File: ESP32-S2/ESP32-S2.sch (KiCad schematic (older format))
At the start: 45 parts, among them IC1 IP4220CZ6, J1 USB_A, J2 TYPE-C-31-M-12, J3 Conn_01x18_Male, J4 S2B-PH-SM4-TB(LF)(SN), J5 Conn_01x22_Male, SW1 SW_Push, SW2 SW_Push, U1 ESP32-S2-WROOM-ESP32-S2-WROOM, U2 MMBT8050, U3 MMBT8050, U4 MCP73831-2-OT, U5 AMS1117-3.3, U6 CH340C

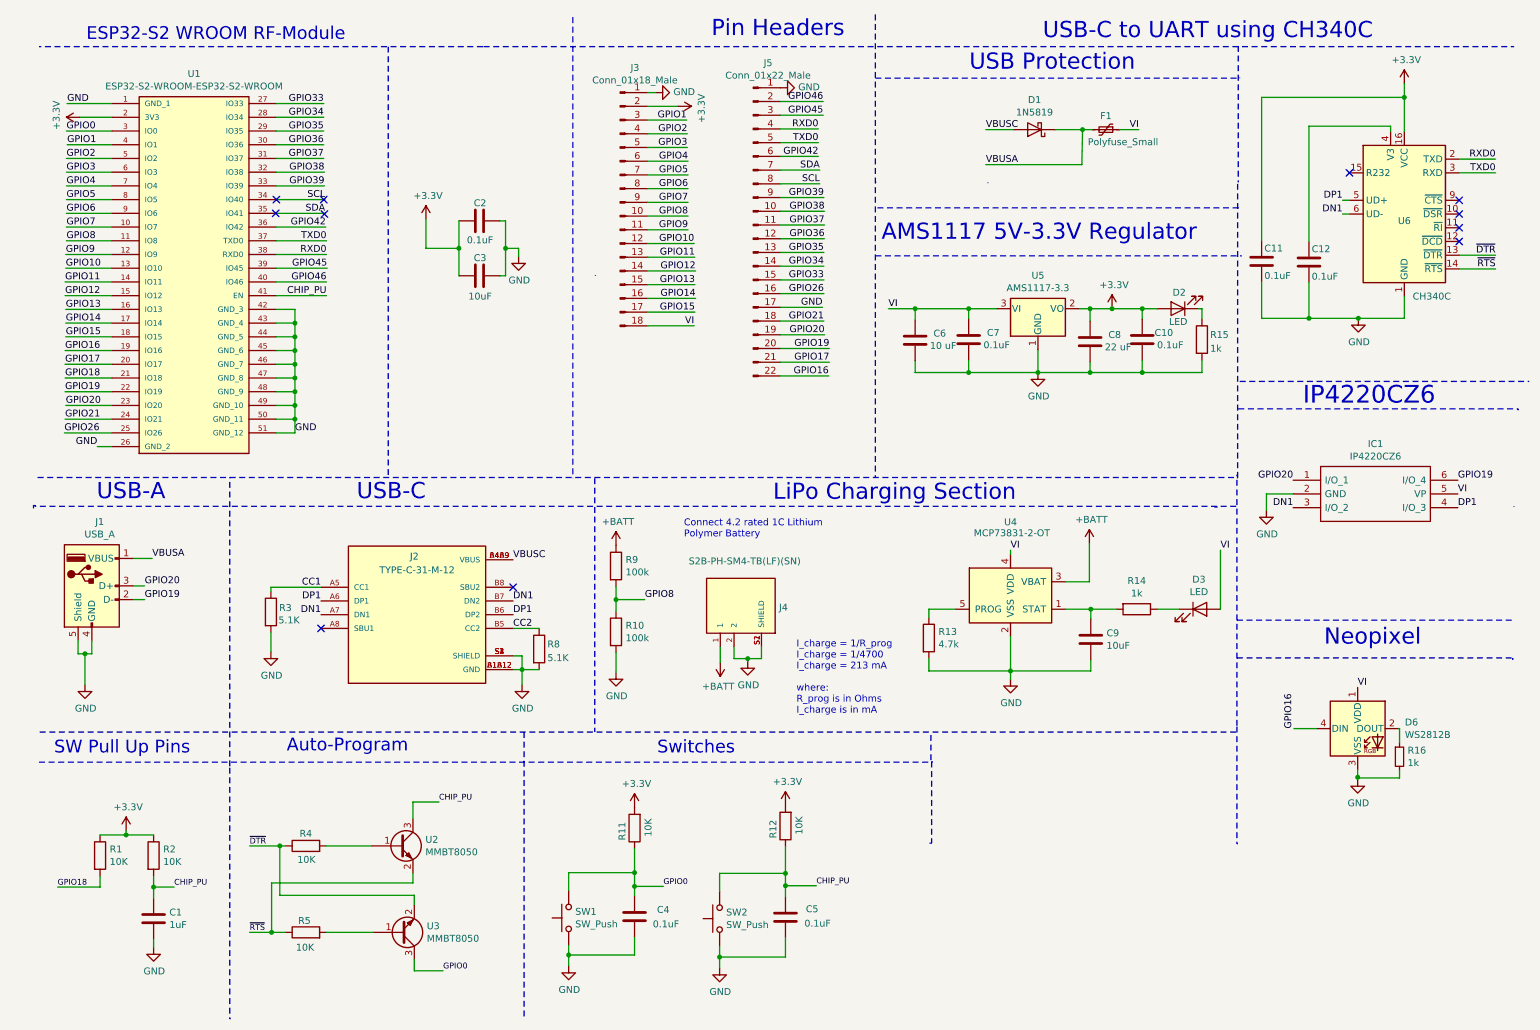
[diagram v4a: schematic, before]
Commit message: Routed 4-layer v.2.1
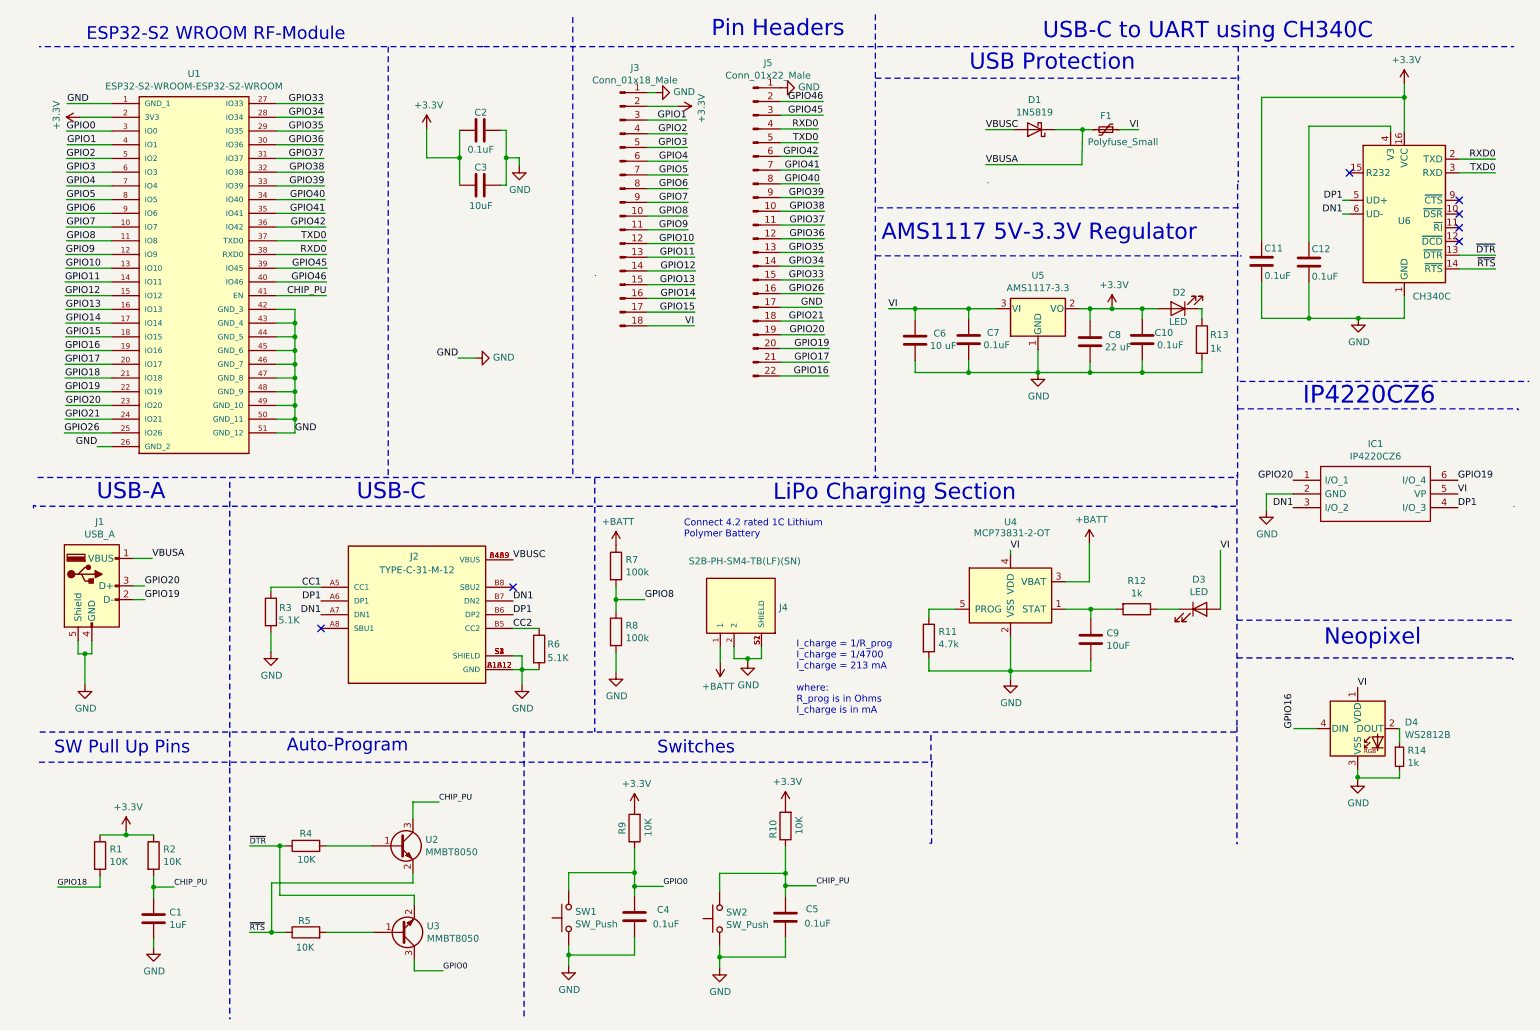
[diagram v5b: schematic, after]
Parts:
- renumbered D6 to D4, R12 to R10, R13 to R11, R14 to R12, R15 to R13, R16 to R14, R8 to R6, R9 to R7, R10 to R8, R11 to R9
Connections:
- net SCL renamed GPIO40
- net SDA renamed GPIO41
- no-connect marks 11 -> 7
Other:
- moved on the sheet: C2, C3
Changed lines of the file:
@@
 GPIO0
 Wire Wire Line
-	3830 1985 3870 1985
-Wire Wire Line
-	3290 2185 3530 2185
-Wire Wire Line
-	3290 1975 3290 2185
-Wire Wire Line
-	3530 2185 3530 2385
-Connection ~ 3530 2185
-Wire Wire Line
-	3530 1985 3530 2185
+	3835 1325 3875 1325
+Wire Wire Line
+	3295 1525 3535 1525
+Wire Wire Line
+	3295 1315 3295 1525
+Wire Wire Line
+	3535 1525 3535 1725
+Connection ~ 3535 1525
+Wire Wire Line
+	3535 1325 3535 1525
 $Comp
 L power:+3.3V #PWR06
 U 1 1 6005C874
-P 3290 1975
-F 0 "#PWR06" H 3290 1825 50  0001 C CNN
-F 1 "+3.3V" H 3305 2148 50  0000 C CNN
-F 2 "" H 3290 1975 50  0001 C CNN
-F 3 "" H 3290 1975 50  0001 C CNN
-	1    3290 1975
+P 3295 1315
+F 0 "#PWR06" H 3295 1165 50  0001 C CNN
+F 1 "+3.3V" H 3310 1488 50  0000 C CNN
+F 2 "" H 3295 1315 50  0001 C CNN
+F 3 "" H 3295 1315 50  0001 C CNN
+	1    3295 1315
 	1    0    0    -1
 $EndComp
@@
 L Device:C C2
 U 1 1 60022F39
-P 3680 1985
-F 0 "C2" V 3810 1935 50  0000 L CNN
-F 1 "0.1uF" V 3540 1885 50  0000 L CNN
-F 2 "Capacitor_SMD:C_0603_1608Metric" H 3718 1835 50  0001 C CNN
-F 3 "~" H 3680 1985 50  0001 C CNN
-	1    3680 1985
+P 3685 1325
+F 0 "C2" V 3815 1275 50  0000 L CNN
+F 1 "0.1uF" V 3545 1225 50  0000 L CNN
+F 2 "Capacitor_SMD:C_0603_1608Metric" H 3723 1175 50  0001 C CNN
+F 3 "~" H 3685 1325 50  0001 C CNN
+	1    3685 1325
 	0    -1   -1   0
 $EndComp
@@
 L Device:C C3
 U 1 1 60021E18
-P 3680 2385
-F 0 "C3" V 3810 2335 50  0000 L CNN
-F 1 "10uF" V 3530 2295 50  0000 L CNN
-F 2 "Capacitor_SMD:C_0603_1608Metric" H 3718 2235 50  0001 C CNN
-F 3 "~" H 3680 2385 50  0001 C CNN
-	1    3680 2385
+P 3685 1725
+F 0 "C3" V 3815 1675 50  0000 L CNN
+F 1 "10uF" V 3535 1635 50  0000 L CNN
+F 2 "Capacitor_SMD:C_0603_1608Metric" H 3723 1575 50  0001 C CNN
+F 3 "~" H 3685 1725 50  0001 C CNN
+	1    3685 1725
 	0    -1   -1   0
 $EndComp
@@
 Wire Wire Line
 	2200 2030 2560 2030
-Wire Wire Line
-	2200 1930 2555 1930
-Text Label 2555 1930 2    50   ~ 0
-SDA
-Wire Wire Line
-	2200 1830 2555 1830
-Text Label 2555 1830 2    50   ~ 0
-SCL
 Text Label 2565 2430 2    50   ~ 0
 GPIO46
@@
 	430  4055 430  4080
 Wire Wire Line
-	3870 1985 3870 2185
-$Comp
-L power:GND #PWR09
+	3875 1325 3875 1525
+$Comp
+L power:GND #PWR08
 U 1 1 600B09CA
-P 3965 2245
-F 0 "#PWR09" H 3965 1995 50  0001 C CNN
-F 1 "GND" H 3970 2072 50  0000 C CNN
-F 2 "" H 3965 2245 50  0001 C CNN
-F 3 "" H 3965 2245 50  0001 C CNN
-	1    3965 2245
-	1    0    0    -1
-$EndComp
-Wire Wire Line
-	3965 2185 3870 2185
-Connection ~ 3870 2185
-Wire Wire Line
-	3870 2185 3870 2385
+P 3970 1585
+F 0 "#PWR08" H 3970 1335 50  0001 C CNN
+F 1 "GND" H 3975 1412 50  0000 C CNN
+F 2 "" H 3970 1585 50  0001 C CNN
+F 3 "" H 3970 1585 50  0001 C CNN
+	1    3970 1585
+	1    0    0    -1
+$EndComp
+Wire Wire Line
+	3970 1525 3875 1525
+Connection ~ 3875 1525
+Wire Wire Line
+	3875 1525 3875 1725
 Wire Wire Line
 	2200 3530 2335 3530
@@
 	1000 3630 895  3630
 Wire Wire Line
-	3965 2185 3965 2245
+	3970 1525 3970 1585
 Text Label 895  3630 2    50   ~ 0
 GND
@@
 $EndComp
 $Comp
-L Device:R R11
+L Device:R R9
 U 1 1 60282C1A
 P 4810 6410
-F 0 "R11" V 4900 6365 50  0000 L CNN
+F 0 "R9" V 4900 6365 50  0000 L CNN
 F 1 "10K" V 4710 6340 50  0000 L CNN
 F 2 "Resistor_SMD:R_0603_1608Metric" V 4740 6410 50  0001 C CNN
@@
 CHIP_PU
 $Comp
-L Device:R R12
+L Device:R R10
 U 1 1 602B227B
 P 5910 6395
-F 0 "R12" V 6000 6350 50  0000 L CNN
+F 0 "R10" V 6000 6350 50  0000 L CNN
 F 1 "10K" V 5810 6325 50  0000 L CNN
 F 2 "Resistor_SMD:R_0603_1608Metric" V 5840 6395 50  0001 C CNN
@@
 Wire Wire Line
 	5875 3115 6225 3115
-NoConn ~ 2545 1830
-NoConn ~ 2550 1935
 Wire Wire Line
 	4905 1050 4965 1050
-NoConn ~ 2200 1830
-NoConn ~ 2195 1930
 $Comp
 L Device:R R4
@@
 VBUSC
 $Comp
-L power:GND #PWR08
+L power:GND #PWR09
 U 1 1 606D1B6E
 P 3990 5365
-F 0 "#PWR08" H 3990 5115 50  0001 C CNN
+F 0 "#PWR09" H 3990 5115 50  0001 C CNN
 F 1 "GND" H 3995 5192 50  0000 C CNN
 F 2 "" H 3990 5365 50  0001 C CNN
@@
 $EndComp
 $Comp
-L Device:R R8
+L Device:R R6
 U 1 1 600D9660
 P 4115 5105
-F 0 "R8" H 4175 5140 50  0000 L CNN
+F 0 "R6" H 4175 5140 50  0000 L CNN
 F 1 "5.1K" H 4175 5040 50  0000 L CNN
 F 2 "Resistor_SMD:R_0603_1608Metric" V 4045 5105 50  0001 C CNN
@@
 $EndComp
 Wire Wire Line
-	3830 2385 3870 2385
+	3835 1725 3875 1725
 Wire Wire Line
 	8945 3090 8945 3000
 $Comp
-L Device:R R15
+L Device:R R13
 U 1 1 6033F05F
 P 8945 2850
-F 0 "R15" H 9005 2885 50  0000 L CNN
+F 0 "R13" H 9005 2885 50  0000 L CNN
 F 1 "1k" H 9005 2785 50  0000 L CNN
 F 2 "Resistor_SMD:R_0603_1608Metric" V 8875 2850 50  0001 C CNN
@@
 	4905 2750 5245 2750
 Text Label 6160 1615 2    50   ~ 0
-SDA
+GPIO41
 Text Label 6160 1715 2    50   ~ 0
-SCL
+GPIO40
 Wire Wire Line
 	5875 1615 6160 1615
@@
 $EndComp
 $Comp
-L Device:R_Small R16
+L Device:R_Small R14
 U 1 1 60CA2577
 P 10385 5890
-F 0 "R16" H 10444 5936 50  0000 L CNN
+F 0 "R14" H 10444 5936 50  0000 L CNN
 F 1 "1k" H 10444 5845 50  0000 L CNN
 F 2 "Resistor_SMD:R_0603_1608Metric" H 10385 5890 50  0001 C CNN
@@
 Neopixel
 $Comp
-L Device:R R13
+L Device:R R11
 U 1 1 60A58974
 P 6955 5025
-F 0 "R13" H 7025 5071 50  0000 L CNN
+F 0 "R11" H 7025 5071 50  0000 L CNN
 F 1 "4.7k" H 7025 4980 50  0000 L CNN
 F 2 "Resistor_SMD:R_0603_1608Metric" V 6885 5025 50  0001 C CNN
@@
 $EndComp
 $Comp
-L Device:R R14
+L Device:R R12
 U 1 1 60A59CD2
 P 8470 4815
-F 0 "R14" V 8263 4815 50  0000 C CNN
+F 0 "R12" V 8263 4815 50  0000 C CNN
 F 1 "1k" V 8354 4815 50  0000 C CNN
 F 2 "Resistor_SMD:R_0603_1608Metric" V 8400 4815 50  0001 C CNN
@@
 $EndComp
 $Comp
-L Device:R R10
+L Device:R R8
 U 1 1 60AABA38
 P 4675 4980
-F 0 "R10" H 4745 5026 50  0000 L CNN
+F 0 "R8" H 4745 5026 50  0000 L CNN
 F 1 "100k" H 4745 4935 50  0000 L CNN
 F 2 "Resistor_SMD:R_0603_1608Metric" V 4605 4980 50  0001 C CNN
@@
 $EndComp
 $Comp
-L Device:R R9
+L Device:R R7
 U 1 1 60AC2C56
 P 4675 4500
-F 0 "R9" H 4745 4546 50  0000 L CNN
+F 0 "R7" H 4745 4546 50  0000 L CNN
 F 1 "100k" H 4745 4455 50  0000 L CNN
 F 2 "Resistor_SMD:R_0603_1608Metric" V 4605 4500 50  0001 C CNN
@@
 $EndComp
 $Comp
-L LED:WS2812B D6
+L LED:WS2812B D4
 U 1 1 609FC678
 P 10080 5685
-F 0 "D6" H 10424 5731 50  0000 L CNN
+F 0 "D4" H 10424 5731 50  0000 L CNN
 F 1 "WS2812B" H 10424 5640 50  0000 L CNN
 F 2 "WS2018:WS2812B2020" H 10130 5385 50  0001 L TNN
@@
 	1    0    0    1
 $EndComp
+Text Label 2555 1830 2    50   ~ 0
+GPIO40
+Wire Wire Line
+	2200 1830 2555 1830
+Text Label 2555 1930 2    50   ~ 0
+GPIO41
+Wire Wire Line
+	2200 1930 2555 1930
+$Comp
+L power:GND #PWR07
+U 1 1 60A90427
+P 3650 2985
+F 0 "#PWR07" H 3650 2735 50  0001 C CNN
+F 1 "GND" V 3655 2857 50  0000 R CNN
+F 2 "" H 3650 2985 50  0001 C CNN
+F 3 "" H 3650 2985 50  0001 C CNN
+	1    3650 2985
+	0    -1   -1   0
+$EndComp
+Wire Wire Line
+	3650 2985 3525 2985
+Text Label 3525 2985 2    50   ~ 0
+GND
 $EndSCHEMATC

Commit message: Routing 4-Layer v3.0
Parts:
- C1, C10, C11, C12, C2, C3, C4, C5, C6, C7, C8, C9: symbol Device:C -> ESP32-S2-rescue:C-Device
- D1: symbol Diode:1N5819 -> ESP32-S2-rescue:1N5819-Diode
- D2, D3: symbol Device:LED -> ESP32-S2-rescue:LED-Device
- D4: symbol LED:WS2812B -> ESP32-S2-rescue:WS2812B-LED
- F1: symbol Device:Polyfuse_Small -> ESP32-S2-rescue:Polyfuse_Small-Device
- J3: symbol Connector:Conn_01x18_Male -> ESP32-S2-rescue:Conn_01x18_Male-Connector
- J5: symbol Connector:Conn_01x22_Male -> ESP32-S2-rescue:Conn_01x22_Male-Connector
- R1, R10, R11, R12, R13, R2, R3, R4, R5, R6, R7, R8, R9: symbol Device:R -> ESP32-S2-rescue:R-Device
- R14: symbol Device:R_Small -> ESP32-S2-rescue:R_Small-Device
- SW1, SW2: symbol Switch:SW_Push -> ESP32-S2-rescue:SW_Push-Switch
- U4: symbol Battery_Management:MCP73831-2-OT -> ESP32-S2-rescue:MCP73831-2-OT-Battery_Management
- U5: symbol Regulator_Linear:AMS1117-3.3 -> ESP32-S2-rescue:AMS1117-3.3-Regulator_Linear
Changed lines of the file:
@@
 $EndDescr
 $Comp
-L power:GND #PWR010
+L ESP32-S2-rescue:GND-power #PWR010
 U 1 1 6010A754
 P 4330 7415
@@
 $EndComp
 $Comp
-L power:GND #PWR016
+L ESP32-S2-rescue:GND-power #PWR016
 U 1 1 6010BC5F
 P 5430 7430
@@
 	5430 7270 5430 7350
 $Comp
-L Device:C C4
+L ESP32-S2-rescue:C-Device C4
 U 1 1 60115502
 P 4810 7055
@@
 $EndComp
 $Comp
-L Device:C C5
+L ESP32-S2-rescue:C-Device C5
 U 1 1 60116DC7
 P 5910 7060
@@
 	3535 1325 3535 1525
 $Comp
-L power:+3.3V #PWR06
+L ESP32-S2-rescue:+3.3V-power #PWR06
 U 1 1 6005C874
 P 3295 1315
@@
 $EndComp
 $Comp
-L Device:C C2
+L ESP32-S2-rescue:C-Device C2
 U 1 1 60022F39
 P 3685 1325
@@
 $EndComp
 $Comp
-L Device:C C3
+L ESP32-S2-rescue:C-Device C3
 U 1 1 60021E18
 P 3685 1725
@@
 GPIO35
 $Comp
-L power:GND #PWR027
+L ESP32-S2-rescue:GND-power #PWR027
 U 1 1 60107D6F
 P 10085 2695
@@
 	3875 1325 3875 1525
 $Comp
-L power:GND #PWR08
+L ESP32-S2-rescue:GND-power #PWR08
 U 1 1 600B09CA
 P 3970 1585
@@
 $EndComp
 $Comp
-L Device:R R9
+L ESP32-S2-rescue:R-Device R9
 U 1 1 60282C1A
 P 4810 6410
@@
 CHIP_PU
 $Comp
-L Device:R R10
+L ESP32-S2-rescue:R-Device R10
 U 1 1 602B227B
 P 5910 6395
@@
 NoConn ~ 10820 1935
 $Comp
-L Device:C C12
+L ESP32-S2-rescue:C-Device C12
 U 1 1 600DA2FD
 P 9725 2285
@@
 	805  5140 855  5140
 $Comp
-L power:GND #PWR02
+L ESP32-S2-rescue:GND-power #PWR02
 U 1 1 6048FF18
 P 805 5365
@@
 	1105 6430 1105 6460
 $Comp
-L power:+3.3V #PWR03
+L ESP32-S2-rescue:+3.3V-power #PWR03
 U 1 1 600E7114
 P 1105 6430
@@
 	1305 7220 1305 7280
 $Comp
-L power:GND #PWR04
+L ESP32-S2-rescue:GND-power #PWR04
 U 1 1 600DA8F4
 P 1305 7280
@@
 $EndComp
 $Comp
-L Device:C C1
+L ESP32-S2-rescue:C-Device C1
 U 1 1 600D7FAA
 P 1305 7070
@@
 $EndComp
 $Comp
-L Device:R R2
+L ESP32-S2-rescue:R-Device R2
 U 1 1 600D7B61
 P 1305 6610
@@
 $EndComp
 $Comp
-L Device:R R1
+L ESP32-S2-rescue:R-Device R1
 U 1 1 600D7356
 P 915 6610
@@
 	4905 1250 5190 1250
 $Comp
-L power:GND #PWR014
+L ESP32-S2-rescue:GND-power #PWR014
 U 1 1 60579A17
 P 4965 1050
@@
 	4905 1050 4965 1050
 $Comp
-L Device:R R4
+L ESP32-S2-rescue:R-Device R4
 U 1 1 6015B31B
 P 2415 6540
@@
 $EndComp
 $Comp
-L Device:R R5
+L ESP32-S2-rescue:R-Device R5
 U 1 1 6015D1FA
 P 2415 7170
@@
 Auto-Program\n
 $Comp
-L power:+3.3V #PWR020
+L ESP32-S2-rescue:+3.3V-power #PWR020
 U 1 1 602B0D1F
 P 5910 6245
@@
 $EndComp
 $Comp
-L power:+3.3V #PWR013
+L ESP32-S2-rescue:+3.3V-power #PWR013
 U 1 1 602AFFC8
 P 4810 6260
@@
 VBUSC
 $Comp
-L power:GND #PWR09
+L ESP32-S2-rescue:GND-power #PWR09
 U 1 1 606D1B6E
 P 3990 5365
@@
 $EndComp
 $Comp
-L Device:R R6
+L ESP32-S2-rescue:R-Device R6
 U 1 1 600D9660
 P 4115 5105
@@
 $EndComp
 $Comp
-L Device:R R3
+L ESP32-S2-rescue:R-Device R3
 U 1 1 600D889F
 P 2160 4835
@@
 Pin Headers
 $Comp
-L Regulator_Linear:AMS1117-3.3 U5
+L ESP32-S2-rescue:AMS1117-3.3-Regulator_Linear U5
 U 1 1 6028A484
 P 7750 2625
@@
 VI
 $Comp
-L Device:C C7
+L ESP32-S2-rescue:C-Device C7
 U 1 1 60322108
 P 7245 2850
@@
 	8050 2625 8130 2625
 $Comp
-L power:GND #PWR022
+L ESP32-S2-rescue:GND-power #PWR022
 U 1 1 604487CE
 P 7750 3090
@@
 $EndComp
 $Comp
-L power:+3.3V #PWR024
+L ESP32-S2-rescue:+3.3V-power #PWR024
 U 1 1 60463D39
 P 8290 2625
@@
 	8945 3090 8945 3000
 $Comp
-L Device:R R13
+L ESP32-S2-rescue:R-Device R13
 U 1 1 6033F05F
 P 8945 2850
@@
 $EndComp
 $Comp
-L Connector:Conn_01x18_Male J3
+L ESP32-S2-rescue:Conn_01x18_Male-Connector J3
 U 1 1 602F510C
 P 4705 1850
@@
 Connection ~ 8290 2625
 $Comp
-L Device:LED D2
+L ESP32-S2-rescue:LED-Device D2
 U 1 1 602D9272
 P 8770 2625
@@
 	8290 2625 8510 2625
 $Comp
-L Device:C C10
+L ESP32-S2-rescue:C-Device C10
 U 1 1 6084EB48
 P 8510 2850
@@
 GND
 $Comp
-L Switch:SW_Push SW1
+L ESP32-S2-rescue:SW_Push-Switch SW1
 U 1 1 6035F446
 P 4330 7065
@@
 $EndComp
 $Comp
-L Switch:SW_Push SW2
+L ESP32-S2-rescue:SW_Push-Switch SW2
 U 1 1 60360186
 P 5430 7070
@@
 	4115 4955 3925 4955
 $Comp
-L power:GND #PWR05
+L ESP32-S2-rescue:GND-power #PWR05
 U 1 1 60667EC7
 P 2160 5125
@@
 	10320 1335 10320 1295
 $Comp
-L power:+3.3V #PWR028
+L ESP32-S2-rescue:+3.3V-power #PWR028
 U 1 1 60C81F04
 P 10420 985
@@
 	10420 1335 10420 1085
 $Comp
-L Connector:Conn_01x22_Male J5
+L ESP32-S2-rescue:Conn_01x22_Male-Connector J5
 U 1 1 60CCC92A
 P 5675 2015
@@
 	5875 2915 6230 2915
 $Comp
-L Device:C C11
+L ESP32-S2-rescue:C-Device C11
 U 1 1 60DF3BEA
 P 9380 2280
@@
 	4905 1150 5125 1150
 $Comp
-L power:GND #PWR019
+L ESP32-S2-rescue:GND-power #PWR019
 U 1 1 6111F61D
 P 5875 1015
@@
 	4525 2380 4525 2385
 $Comp
-L Device:C C6
+L ESP32-S2-rescue:C-Device C6
 U 1 1 605779A1
 P 6855 2855
@@
 $EndComp
 $Comp
-L Device:C C8
+L ESP32-S2-rescue:C-Device C8
 U 1 1 60577F9E
 P 8130 2865
@@
 	9200 5665 9200 3835
 $Comp
-L Battery_Management:MCP73831-2-OT U4
+L ESP32-S2-rescue:MCP73831-2-OT-Battery_Management U4
 U 1 1 6069F730
 P 7550 4715
@@
 	8345 1320 8485 1320
 $Comp
-L Device:Polyfuse_Small F1
+L ESP32-S2-rescue:Polyfuse_Small-Device F1
 U 1 1 6047A0CA
 P 8245 1320
@@
 VI
 $Comp
-L power:GND #PWR026
+L ESP32-S2-rescue:GND-power #PWR026
 U 1 1 60C5B2E2
 P 10080 6055
@@
 $EndComp
 $Comp
-L Device:R_Small R14
+L ESP32-S2-rescue:R_Small-Device R14
 U 1 1 60CA2577
 P 10385 5890
@@
 	10385 5990 10385 6045
 $Comp
-L Diode:1N5819 D1
+L ESP32-S2-rescue:1N5819-Diode D1
 U 1 1 60956142
 P 7725 1320
@@
 VI
 $Comp
-L power:GND #PWR025
+L ESP32-S2-rescue:GND-power #PWR025
 U 1 1 60A14DD4
 P 9415 4095
@@
 Neopixel
 $Comp
-L Device:R R11
+L ESP32-S2-rescue:R-Device R11
 U 1 1 60A58974
 P 6955 5025
@@
 $EndComp
 $Comp
-L Device:C C9
+L ESP32-S2-rescue:C-Device C9
 U 1 1 60A59496
 P 8135 5035
@@
 $EndComp
 $Comp
-L Device:R R12
+L ESP32-S2-rescue:R-Device R12
 U 1 1 60A59CD2
 P 8470 4815
@@
 $EndComp
 $Comp
-L Device:LED D3
+L ESP32-S2-rescue:LED-Device D3
 U 1 1 60A5A83D
 P 8930 4815
@@
 $EndComp
 $Comp
-L power:GND #PWR021
+L ESP32-S2-rescue:GND-power #PWR021
 U 1 1 60A5C71F
 P 7550 5325
@@
 $EndComp
 $Comp
-L power:GND #PWR012
+L ESP32-S2-rescue:GND-power #PWR012
 U 1 1 60A9405E
 P 4675 5275
@@
 $EndComp
 $Comp
-L Device:R R8
+L ESP32-S2-rescue:R-Device R8
 U 1 1 60AABA38
 P 4675 4980
@@
 $EndComp
 $Comp
-L Device:R R7
+L ESP32-S2-rescue:R-Device R7
 U 1 1 60AC2C56
 P 4675 4500
@@
 $EndComp
 $Comp
-L power:+BATT #PWR017
+L ESP32-S2-rescue:+BATT-power #PWR017
 U 1 1 60ADA7D5
 P 5435 5205
@@
 	5735 5175 5735 5090
 $Comp
-L power:GND #PWR018
+L ESP32-S2-rescue:GND-power #PWR018
 U 1 1 60B24C40
 P 5635 5195
@@
 	9080 4385 9080 4815
 $Comp
-L power:+BATT #PWR023
+L ESP32-S2-rescue:+BATT-power #PWR023
 U 1 1 60DACAED
 P 8125 4335
@@
 VI
 $Comp
-L power:+BATT #PWR011
+L ESP32-S2-rescue:+BATT-power #PWR011
 U 1 1 60E23FFD
 P 4675 4350
@@
 Connect 4.2 rated 1C Lithium\nPolymer Battery
 $Comp
-L power:+3.3V #PWR01
+L ESP32-S2-rescue:+3.3V-power #PWR01
 U 1 1 610BFFB6
 P 770 1230
@@
 	770  1230 1000 1230
 $Comp
-L power:+3.3V #PWR015
+L ESP32-S2-rescue:+3.3V-power #PWR015
 U 1 1 60AF9A04
 P 5125 1150
@@
 $EndComp
 $Comp
-L LED:WS2812B D4
+L ESP32-S2-rescue:WS2812B-LED D4
 U 1 1 609FC678
 P 10080 5685
@@
 	2200 1930 2555 1930
 $Comp
-L power:GND #PWR07
+L ESP32-S2-rescue:GND-power #PWR07
 U 1 1 60A90427
 P 3650 2985
